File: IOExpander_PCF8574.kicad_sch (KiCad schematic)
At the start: 21 parts, among them J1 Conn_01x04_Pin, J2 Conn_01x08_Pin, J3 Conn_01x08_Pin, U1 PCF8574, U2 PCF8574

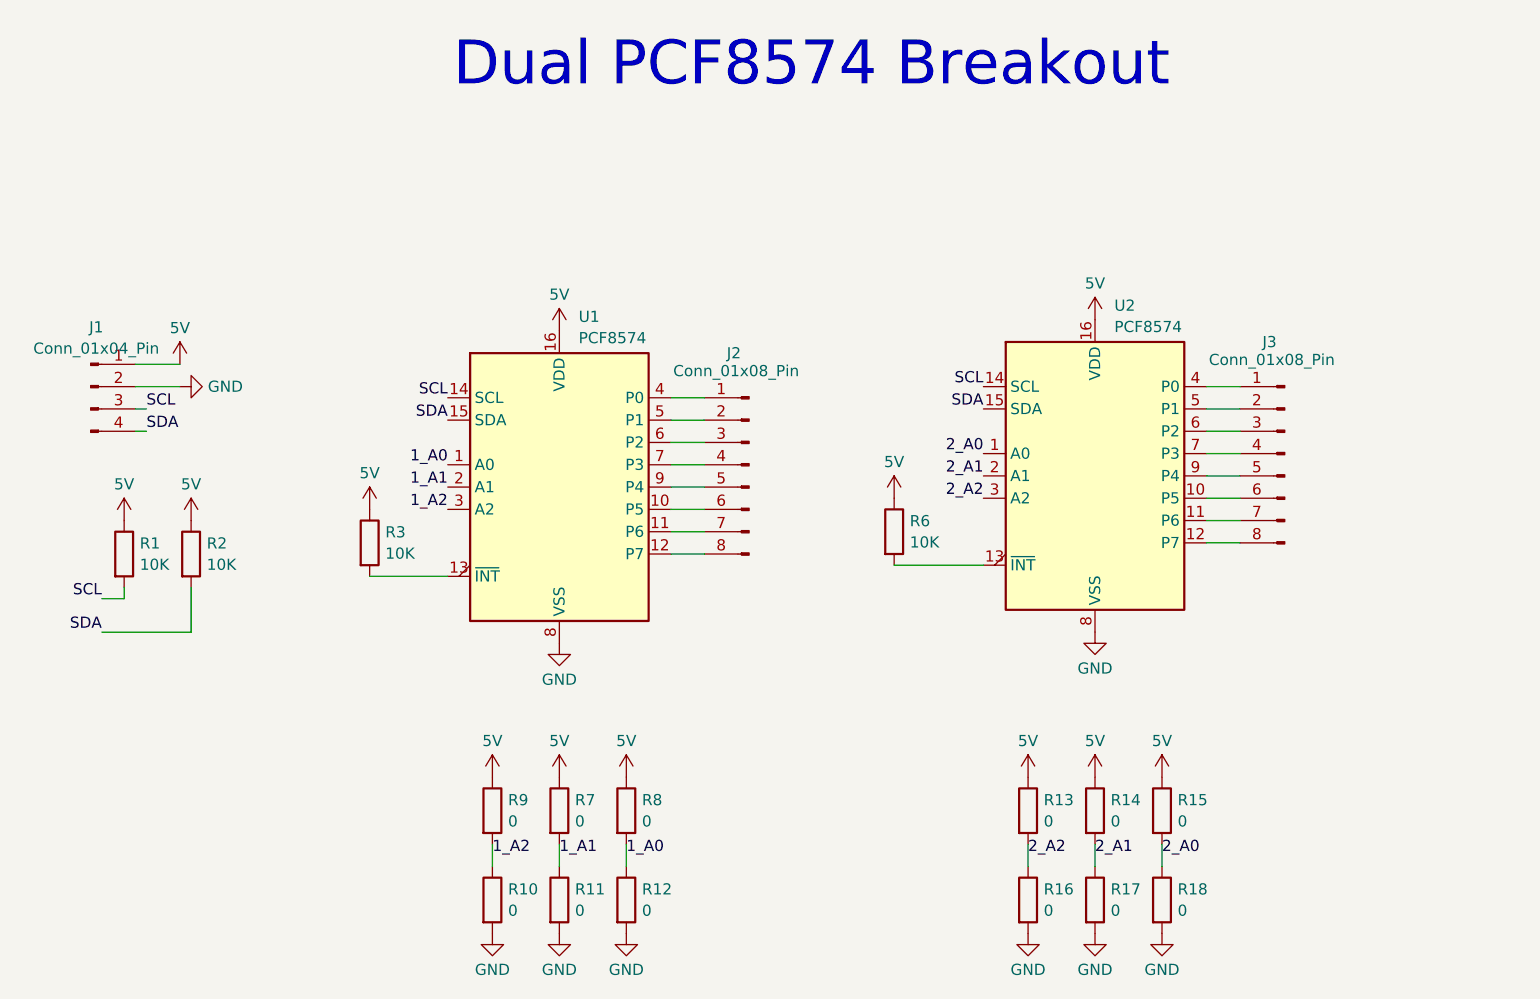
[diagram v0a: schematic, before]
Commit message: Coupling Capacitors added
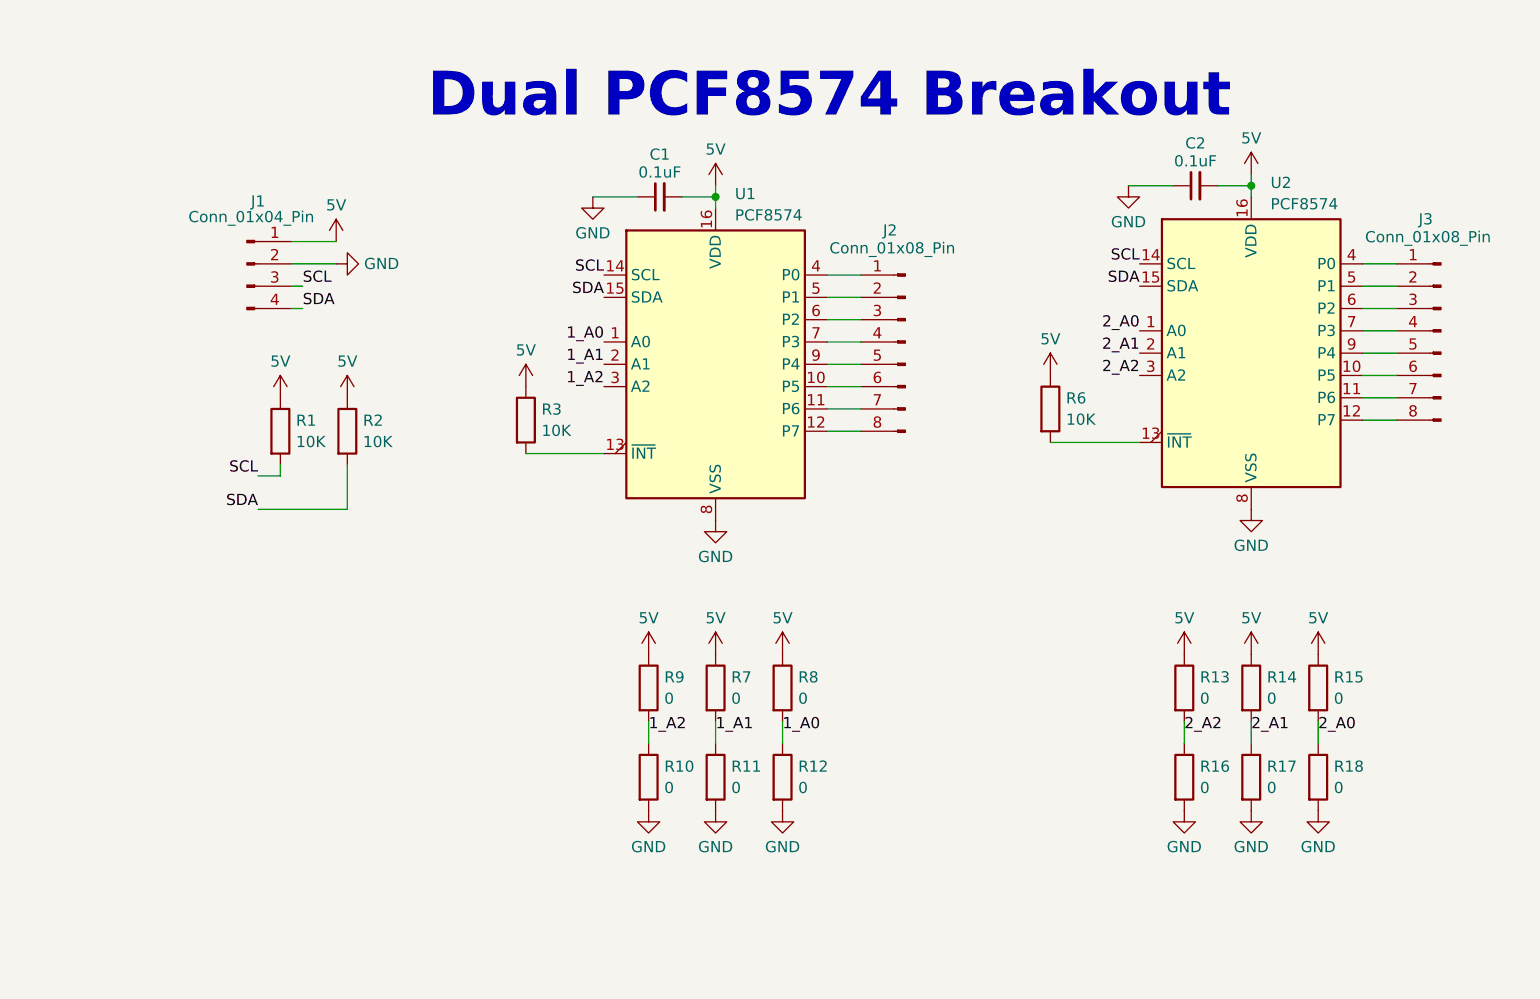
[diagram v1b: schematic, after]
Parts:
- added C1, C2: 0.1uF, Capacitor_SMD:C_1206_3216Metric_Pad1.33x1.80mm_HandSolder, symbol Device:C_Small
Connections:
- net 5V: now also C1.2, C2.2
- net GND: now also C1.1, C2.1
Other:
- moved on the sheet: J1, J2, J3, R1, R10, R11, R12, R13, R14, R15, R16, R17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

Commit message: editing the footprint of PCF8574
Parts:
- U1, U2: footprint Package_SO:SOP-16_4.4x10.4mm_P1.27mm -> Package_SO:SO-16_5.3x10.2mm_P1.27mm
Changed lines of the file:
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@@
 			)
 		)
-		(property "Footprint" "Package_SO:SOP-16_4.4x10.4mm_P1.27mm"
+		(property "Footprint" "Package_SO:SO-16_5.3x10.2mm_P1.27mm"
 			(at 199.39 64.77 0)
 			(effects
@@
 			)
 		)
-		(property "Footprint" "Package_SO:SOP-16_4.4x10.4mm_P1.27mm"
+		(property "Footprint" "Package_SO:SO-16_5.3x10.2mm_P1.27mm"
 			(at 138.43 66.04 0)
 			(effects

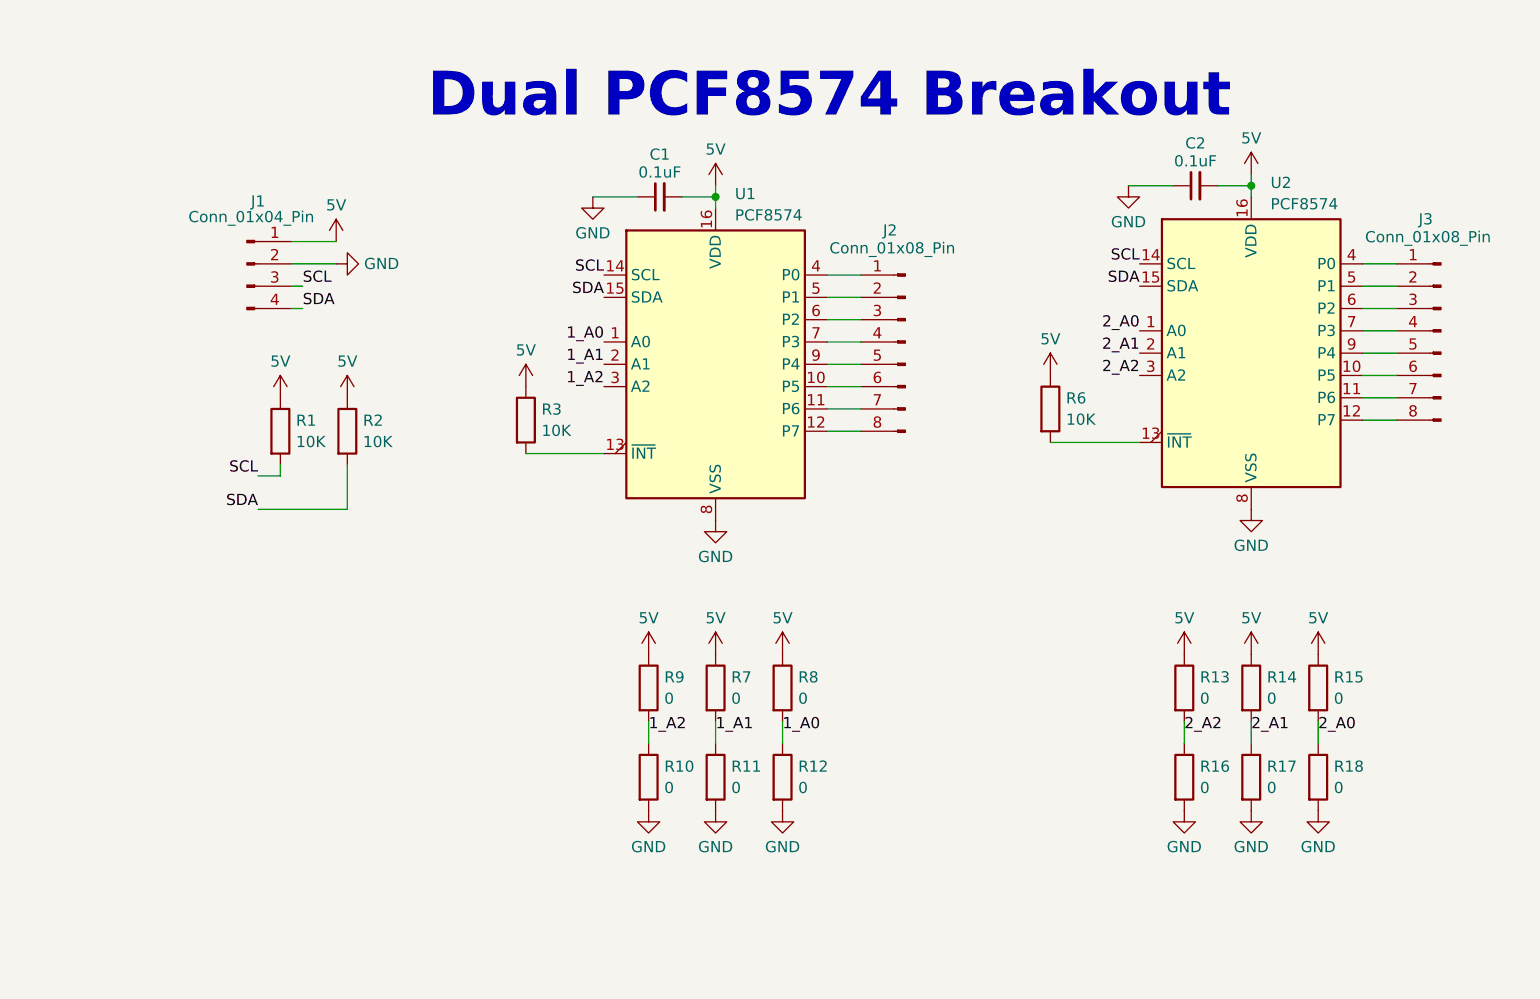
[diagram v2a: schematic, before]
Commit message: Pull Up resistors are added for each channel
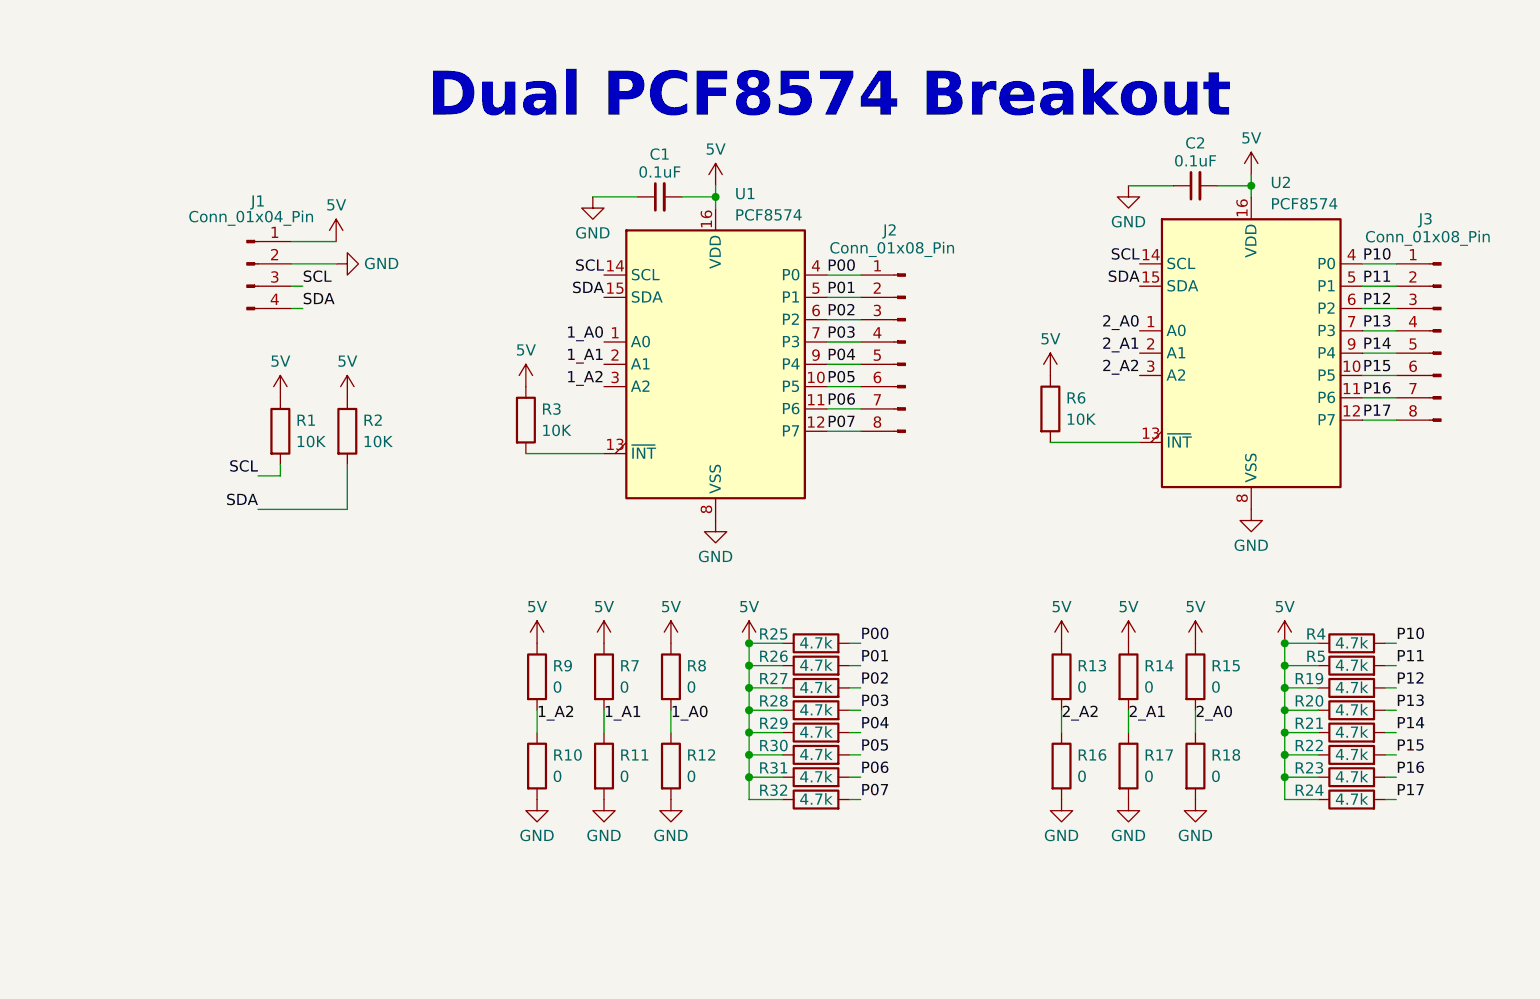
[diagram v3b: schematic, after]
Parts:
- added R19, R20, R21, R22, R23, R24, R25, R26, R27, R28, R29, R30, R31, R32, R4, R5: 4.7k, Resistor_SMD:R_1206_3216Metric_Pad1.30x1.75mm_HandSolder, symbol Device:R
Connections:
- net 5V: now also R19.1, R20.1, R21.1, R22.1, R23.1, R24.1, R25.1, R26.1, R27.1, R28.1, R29.1, R30.1, R31.1, R32.1, R4.1, R5.1
- net P10: now reaches J3.1 (Pin_1), U2.4 (P0)
- net P10: now also R4.2
- net P11: now reaches J3.2 (Pin_2), U2.5 (P1)
- net P11: now also R5.2
- net P12: now reaches J3.3 (Pin_3), U2.6 (P2)
- net P12: now also R19.2
- net P13: now reaches J3.4 (Pin_4), U2.7 (P3)
- net P13: now also R20.2
- net P14: now reaches J3.5 (Pin_5), U2.9 (P4)
- net P14: now also R21.2
- net P15: now reaches J3.6 (Pin_6), U2.10 (P5)
- net P15: now also R22.2
- net P16: now reaches J3.7 (Pin_7), U2.11 (P6)
- net P16: now also R23.2
- net P17: now reaches J3.8 (Pin_8), U2.12 (P7)
- net P17: now also R24.2
- net P05: now reaches J2.6 (Pin_6), U1.10 (P5)
- net P05: now also R30.2
- net P06: now reaches J2.7 (Pin_7), U1.11 (P6)
- net P06: now also R31.2
- net P07: now reaches J2.8 (Pin_8), U1.12 (P7)
- net P07: now also R32.2
- net P00: now reaches J2.1 (Pin_1), U1.4 (P0)
- net P00: now also R25.2
- net P01: now reaches J2.2 (Pin_2), U1.5 (P1)
- net P01: now also R26.2
- net P02: now reaches J2.3 (Pin_3), U1.6 (P2)
- net P02: now also R27.2
- net P03: now reaches J2.4 (Pin_4), U1.7 (P3)
- net P03: now also R28.2
- net P04: now reaches J2.5 (Pin_5), U1.9 (P4)
- net P04: now also R29.2
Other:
- moved on the sheet: R10, R11, R12, R13, R14, R15, R16, R17, R18, R7, R8, R9
